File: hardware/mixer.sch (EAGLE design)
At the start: 86 parts, among them IC1 PGA2311, IC2 PGA2311, IC3 PGA2311, IC4 PGA2311, IC5 PGA2311, IC6 OPA2336U, K1 RT424F124, K2 RT424F124, Q1 si2305cd, Q3 IRLML9301, Q4 IRLML9301, Q5 IRLML9301, Q7 IRLML9301, T1 BC846, T2 BC846, T3 BC846, T4 BC846, U1 SPX5205 3v3, Y1 32768Hz CFPX-217 12.5pF

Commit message: add png
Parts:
- removed C23: 22pF, rcl:C-EUC0805
- removed D1, D2, D3, D4: M4, SparkFun-DiscreteSemi:DIODESMA
- removed K1, K2: RT424F124, relay:RT424F124
- removed LED1: green, led:LEDCHIP-LED0805
- removed LED2: orange, led:LEDCHIP-LED0805
- removed Q1: si2305cd, Simplex-DiscreteSemi:MOSFET-PCHANNELSMD_POWER
- removed Q3, Q4, Q5, Q7: IRLML9301, Simplex-DiscreteSemi:MOSFET-PCHANNELSMD_POWER
- removed R22: 8.2K, rcl:R-EU_R0805W
- removed R27: 1K, rcl:R-EU_R0805W
- removed T1, T2, T3, T4: BC846, transistor:BC846
- removed U1: SPX5205 3v3, SparkFun:V_REG_LDOSMD
- removed Y1: 32768Hz CFPX-217 12.5pF, Simplex-FreqCtrl:CRYSTAL3.2X1.5
- added C15, C16, C18, C55, C57, C59, C61, C63: 47p, rcl:C-EUC0805
- added C19, C21, C22, C25, C26, C28, C29, C30, C31, C32, C33, C34, C35, C36, C37, C38, C39, C40, C41, C42, C43, C44, C46, C47, C48, C49, C51, C52, C53, C54, C79, C80: 100n, rcl:C-EUC0805
- added C56, C58, C60, C62, C64, C65, C66, C67, C68, C69, C70, C71, C72, C73, C74, C75, C76, C77, C78: 10u, SparkFun-Capacitors:CAP_POLD
- added IC11, IC12, IC7, IC8, IC9: OPA2134P, burr-brown:OPA2134P
- added R41, R43, R45: 47K, rcl:R-EU_R0805W
- added R42, R44: 1K, rcl:R-EU_R0805W
- added U$2: INDUCTOR, Simplex-rlc:INDUCTOR
- added U$3: RESETTABLE, Simplex-Fuses:RESETTABLE
- added U$5: MOLEX_4HORIZONTAL, Simplex-Connectors:MOLEX_4HORIZONTAL
- C1, C13, C14, C5, C6, C9: value 100nF -> 100n
- C10: value 470nF -> 100n
- C11: value 220nF -> 47p
- C12, C17, C7, C8: value 100nF -> 47p
- C2, C20: value 10uF -> 100n; device rcl:C-EUC1206 -> rcl:C-EUC0805
- C24: value 22pF -> 100n
- C3: value 10uF -> 47p; device rcl:C-EUC1206 -> rcl:C-EUC0805
- C4: value 1uF -> 47p
- IC6: value OPA2336U -> OPA2134P; device burr-brown:OPA2336U -> burr-brown:OPA2134P
- R1, R11, R20, R3: value 100k -> 47K
- R12, R2, R8: value 10k -> 1K
- R13, R15, R32, R9: value 100K -> 47K
- R14: value 100K -> 1K
- R16: value 100k -> 1K
- R17: value 8K -> 22K
- R18, R24, R25, R28: value 20K -> 47K
- R19, R21: value 10k -> 47K
- R23: value 160K -> 22K
- R26: value 8K -> 47K
- R29: value 8.2K -> 22K
- R30: value 160K -> 47K
- R31: value 68K -> 10
- R33: value 50 -> 10
- R34: value 47k -> 10
- R35: value 47k -> 22K
- R36, R39: value 470 -> 47K
- R37, R38: value 470 -> 10
- R4, R6: value 4.7k -> 1K
- R40: value 50 -> 47K
- R5, R7: value 4.7k -> 47K
- U$1: value F55[0/1]X---PT48 -> INDUCTOR; device TI_MSP430_v16:F55[0/1]X---PT48 -> Simplex-rlc:INDUCTOR
- U$4: value INDUCTOR -> RESETTABLE; device Simplex-rlc:INDUCTOR -> Simplex-Fuses:RESETTABLE
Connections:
- removed net +30V: R30.2
- removed net +3V: R32.2
- removed net +3V3: C1.1, C2.1, U1.OUT
- removed net -30V: R23.2
- removed net 3V: IC6A.V+
- removed net A+3: C14.2, R31.2, R32.1, U$1.5
- removed net A+30: C13.2, R29.2, R30.1, U$1.3
- removed net A+5: C12.2, R26.2, R28.1, U$1.1
- removed net A-30: IC6B.OUT, R25.2, R9.2, U$1.4
- removed net A-5: IC6A.OUT, R13.2, R24.2, U$1.2
- removed net CHARGE_OFF: R20.2, U$1.19
- removed net CHARGE_ON: R16.2, U$1.18
- removed net CS: U$1.35
- removed net EN: R8.1, U$1.20
- removed net GND: C1.2, C10.2, C11.2, C12.1, C13.1, C14.1, C17.1, C2.2, C20.2, C23.2, C24.2, C3.2, C4.2, C5.1, C6.2, C7.1, C8.1, C9.1, IC6A.V-, LED1.C, R17.1, R22.1, R26.1, R27.1, R29.1, R31.1, R33.1, R35.2, R40.1, T1.E, T2.E, T3.E, T4.E, U$1.10, U$1.12, U$1.27, U$1.37, U$1.39, U$1.44, U1.GND
- removed net LED: R10.2, U$1.36
- removed net MISO: U$1.31
- removed net N$13: R7.2, U$1.33
- removed net N$14: Q1.G, R3.1, R8.2
- removed net N$24: C5.2, R15.1, R22.2, R23.1
- removed net N$25: C24.1, U$1.9, Y1.1
- removed net N$3: R16.1, T1.B
- removed net N$35: D3.C, K11.R+, Q7.D, R37.1
- removed net N$39: LED2.C, R27.2
- removed net N$6: C10.1, U$1.13
- removed net P1.0: U$1.14
- removed net P1.1: U$1.15
- removed net P1.2: U$1.16
- removed net P1.3: U$1.17
- removed net P4.0: U$1.29
- removed net RST: R34.1, U$1.48
- removed net RX: R6.1
- removed net R_OFF: R11.2, U$1.22
- removed net R_ON: R1.2, U$1.21
- removed net SCK: U$1.32
- removed net SCL: R4.2
- removed net SDA: R5.2
- removed net TEST: R35.1, U$1.47
- removed net TX: R7.1
- removed net VBAT: Q3.S, Q4.S, Q5.S, Q7.S, R12.1, R19.1, R2.1, R21.1
- removed net VBAT_GND: D1.A, D2.A, D3.A, D4.A, K11.-, K21.-, R36.2, R37.2, R38.2, R39.2
- removed net VCC: C17.2, C8.2, C9.2, Q1.S, R3.2, R34.2, U$1.11, U$1.28, U$1.7
- removed net VCC_EN: C20.1, R4.1, R5.1, U$4.2
- removed net VIN: C3.1, C6.1, U1.EN, U1.IN
- new net AGND: C11.1, C12.1, C15.1, C16.1, C17.1, C18.1, C29.2, C3.1, C30.2, C31.2, C34.2, C35.2, C36.2, C37.2, C38.2, C39.2, C4.1, C40.2, C41.2, C42.2, C43.2, C44.2, C46.2, C47.2, C48.2, C49.2, C51.2, C52.2, C53.2, C54.2, C65.-, C66.-, C67.-, C68.-, C69.-, C7.1, C70.+, C71.+, C72.+, C73.+, C74.+, C75.-, C76.-, C77.+, C78.+, C8.1, IC1.AGNDL, IC1.AGNDR, IC2.AGNDL, IC2.AGNDR, IC3.AGNDL, IC3.AGNDR, IC4.AGNDL, IC4.AGNDR, IC5.AGNDL, IC5.AGNDR, R1.1, R11.1, R13.1, R15.1, R17.1, R23.1, R29.1, R3.1, R35.1, R41.1, R43.1, R5.1, R7.1, R9.1, U$5.3
- new net CLK: IC1.SCLK, IC2.SCLK, IC3.SCLK, IC4.SCLK, IC5.SCLK
- new net CS1: IC1.CS
- new net CS2: IC2.CS
- new net CS3: IC3.CS
- new net CS4: IC4.CS
- new net CS5: IC5.CS
- new net DGND: C55.1, C56.-, C57.1, C58.-, C59.1, C60.-, C61.1, C62.-, C63.1, C64.-, IC1.DGND, IC2.DGND, IC3.DGND, IC4.DGND, IC5.DGND, U$5.2
- new net FRONT_L: C1.1
- new net FRONT_R: C2.1
- new net LINE_L: C9.1
- new net LINE_R: C10.1
- new net M1: IC1.MUTE
- new net M2: IC2.MUTE
- new net M3: IC3.MUTE
- new net M4: IC4.MUTE
- new net M5: IC5.MUTE
- new net M_FRONT_L: C19.1, IC11A.OUT, R18.1
- new net M_FRONT_R: C20.1, IC11B.OUT, R28.1
- new net M_REAR_L: IC12A.OUT, R30.1
- new net M_REAR_R: IC12B.OUT, R40.1
- new net N$29: IC7B.+IN
- new net N$33: C15.2, IC7A.+IN, R41.2, R42.2
- new net N$36: C17.2, IC5.VINL, R13.2, R14.2
- new net N$40: C16.2, R43.2, R44.2
- new net N$42: C19.2, R14.1
- new net N$43: C20.2, R16.1
- new net N$46: IC11A.+IN, R17.2
- new net N$47: IC11A.-IN, R18.2, R19.1, R20.1, R21.1
- new net N$48: C21.1, R19.2
- new net N$49: C24.1, R20.2
- new net N$50: C22.1, R21.2
- new net N$51: IC12B.-IN, R36.1, R40.2, R45.1
- new net N$52: IC11B.+IN, R23.2
- new net N$53: IC11B.-IN, R24.1, R25.1, R26.1, R28.2
- new net N$54: C25.1, R24.2
- new net N$55: C28.1, R25.2
- new net N$56: C26.1, R26.2
- new net N$58: IC12A.+IN, R29.2
- new net N$60: U$1.1, U$3.P$1
- new net N$61: C32.1, R32.2
- new net N$62: U$2.1, U$4.P$1
- new net N$63: U$3.P$2, U$5.1
- new net N$64: IC12B.+IN, R35.2
- new net N$66: C33.1, R36.2
- new net N$67: U$4.P$2, U$5.4
- new net N$68: IC5.VD+, R31.2
- new net N$69: C55.2, C56.+, IC1.VD+, IC1.ZCEN, R38.2
- new net N$70: C57.2, C58.+, IC2.VD+, R37.2
- new net N$71: C59.2, C60.+, IC3.VD+, R34.2
- new net N$72: C61.2, C62.+, IC4.VD+, R33.2
- new net N$73: C63.2, C64.+
- new net N$74: IC12A.-IN, R30.2, R32.1, R39.1
- new net N$75: C79.1, R39.2
- new net N$77: C80.1, R45.2
- new net REAR_L: C5.1
- new net REAR_R: C6.1
- new net SPDIF_L: C13.1
- new net SPDIF_R: C14.1
- new net V_FRONT_L: C24.2, IC1.VOUTL
- new net V_FRONT_R: C28.2, IC1.VOUTR
- new net V_LINE_L: C22.2, IC3.VOUTL
- new net V_LINE_R: C26.2, IC3.VOUTR
- new net V_REAR_L: C32.2, IC2.VOUTL
- new net V_REAR_PAN_L: C79.2, IC5.VOUTL
- new net V_REAR_PAN_R: C80.2, IC5.VOUTR
- new net V_REAR_R: C33.2, IC2.VOUTR
- new net V_SPDIF_L: C21.2, IC4.VOUTL
- new net V_SPDIF_R: C25.2, IC4.VOUTR
- net +5V: now also C29.1, C30.1, C31.1, C34.1, C35.1, C36.1, C37.1, C46.1, C47.1, C48.1, C49.1, C65.+, C66.+, C67.+, C68.+, C69.+, C75.+, C76.+, IC1.VA+, IC11A.V+, IC12A.V+, IC2.VA+, IC3.VA+, IC4.VA+, IC5.VA+, IC6A.V+, IC7A.V+, IC8A.V+, IC9A.V+, R31.1, R33.1, R34.1, R37.1, R38.1, U$1.2; no longer R28.2
- net -5V: now also C38.1, C39.1, C40.1, C41.1, C42.1, C43.1, C44.1, C51.1, C52.1, C53.1, C54.1, C70.-, C71.-, C72.-, C73.-, C74.-, C77.-, C78.-, IC1.VA-, IC11A.V-, IC12A.V-, IC2.VA-, IC3.VA-, IC4.VA-, IC5.VA-, IC6A.V-, IC7A.V-, IC8A.V-, IC9A.V-, U$2.2; no longer R18.2, R24.1, R25.1
- net MOSI: now also IC1.SDI, IC2.SDI, IC3.SDI, IC4.SDI, IC5.SDI; no longer U$1.30
- net N$1: now also C1.2, R42.1; no longer LED1.A, R10.1
- net N$10: now also C4.2, R3.2, R4.2; no longer Q3.G, R2.2, T2.C
- net N$11: now also C5.2, R2.1; no longer R6.2, U$1.34
- net N$12: now also C6.2, R4.1; no longer D1.C, K21.S+, Q3.D, R38.1
- net N$15: now also IC3.VINL, IC8A.-IN, IC8A.OUT; no longer R11.1, T4.B
- net N$16: now also IC3.VINR, IC8B.-IN, IC8B.OUT; no longer Q5.G, R12.2, T4.C
- net N$17: now also IC7B.-IN, IC7B.OUT
- net N$18: now also IC8B.+IN; no longer D4.C, K21.R+, Q5.D, R36.1
- net N$19: now also IC9A.-IN, IC9A.OUT; no longer IC2.VINL, IC2.VINR, IC2.VOUTL, IC2.VOUTR, IC3.VINL, IC3.VINR, IC3.VOUTL, IC3.VOUTR, IC4.VINR, IC4.VOUTL, IC4.VOUTR, IC5.VINL, IC5.VINR, IC5.VOUTL, IC5.VOUTR
- net N$2: now also C2.2, R44.1; no longer C4.1, U1.BP
- net N$20: now also C7.2, IC8A.+IN, R5.2, R6.2; no longer IC6A.-IN, R13.1, R14.2
- net N$21: now also C8.2, R7.2, R8.2; no longer IC6B.-IN, R15.2, R9.1
- net N$22: now also C9.2, R6.1; no longer IC6A.+IN, R33.2
- net N$23: now also C10.2, R8.1; no longer IC6B.+IN, R40.2
- net N$26: now also IC4.VINR, IC9B.-IN, IC9B.OUT; no longer C23.1, U$1.8, Y1.2
- net N$27: now also IC9B.+IN; no longer C7.2, R14.1, R17.2, R18.1
- net N$28: now also C11.2, IC9A.+IN, R10.2, R9.2; no longer Q4.G, R19.2, T1.C
- net N$30: now also C12.2, R11.2, R12.2; no longer D2.C, K11.S+, Q4.D, R39.1
- net N$31: now also C13.2, R10.1; no longer R20.1, T3.B
- net N$32: now also C14.2, R12.1; no longer Q7.G, R21.2, T3.C
- net N$37: now also C18.2, IC5.VINR, R15.2, R16.2; no longer Q1.D, U$4.1
- net N$4: now also IC2.VINL, IC6A.-IN, IC6A.OUT; no longer IC1.VOUTL
- net N$5: now also IC7A.-IN, IC7A.OUT
- net N$7: now also IC2.VINR, IC6B.-IN, IC6B.OUT; no longer C11.1, U$1.43
- net N$8: now also IC6B.+IN; no longer R1.1, T2.B
- net N$9: now also C3.2, IC6A.+IN, R1.2, R2.2; no longer IC1.VOUTR
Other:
- note added: "front"
- note added: "front to rear pan"
- note added: "line in"
- note added: "rear"
- note added: "spdif"
- note removed: "uC pins: 7 11 28"
- moved on the sheet: C1, C10, C11, C12, C13, C14, C17, C2, C20, C24, C3, C4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

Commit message: power tweaked
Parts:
- removed C55, C57, C59, C61, C63: 47p, rcl:C-EUC0805
- removed C56, C58, C60, C62, C64: 10u, SparkFun-Capacitors:CAP_POLD
- removed R31, R33, R34, R37, R38: 10, rcl:R-EU_R0805W
- added C45, C50, C81, C82, C83, C84, C85, C86: 100n, rcl:C-EUC0805
- added C87, C88, C89, C90, C91, C94: 10u, SparkFun-Capacitors:CAP_POLD
- added U$10, U$8: RESETTABLE, Simplex-Fuses:RESETTABLE
- added U$6, U$9: bead, Simplex-rlc:INDUCTOR
- U$1, U$2: value INDUCTOR -> bead
- U$5: value MOLEX_4HORIZONTAL -> MOLEX_6HORIZONTAL; device Simplex-Connectors:MOLEX_4HORIZONTAL -> Simplex-Connectors:MOLEX_6HORIZONTAL
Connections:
- net -5V renamed A-5V
- removed net N$10: C4.2, R3.2, R4.2
- removed net N$21: C8.2, R7.2, R8.2
- removed net N$30: C12.2, R11.2, R12.2
- removed net N$40: C16.2, R43.2, R44.2
- removed net N$67: U$4.P$2, U$5.4
- removed net N$68: IC5.VD+, R31.2
- removed net N$69: C55.2, C56.+, IC1.VD+, IC1.ZCEN, R38.2
- removed net N$70: C57.2, C58.+, IC2.VD+, R37.2
- removed net N$71: C59.2, C60.+, IC3.VD+, R34.2
- removed net N$72: C61.2, C62.+, IC4.VD+, R33.2
- removed net N$73: C63.2, C64.+
- new net +3V: C84.1, C85.1, C86.1, C87.-, U$9.2
- new net A+5V: C29.1, C30.1, C31.1, C34.1, C35.1, C36.1, C37.1, C46.1, C47.1, C48.1, C49.1, C65.+, C66.+, C67.+, C68.+, C69.+, C75.+, C76.+, IC1.VA+, IC11A.V+, IC12A.V+, IC2.VA+, IC3.VA+, IC4.VA+, IC5.VA+, IC6A.V+, IC7A.V+, IC8A.V+, IC9A.V+, U$1.2
- new net N$24: U$4.P$2, U$5.3
- new net N$25: U$5.4, U$8.P$2
- new net N$3: U$6.1, U$8.P$1
- new net N$34: U$10.P$2, U$5.5
- new net N$6: U$10.P$1, U$9.1
- net +5V: now also C45.1, C50.1, C81.1, C82.1, C83.1, C88.-, C89.-, C90.-, C91.-, C94.-, IC1.VD+, IC1.ZCEN, IC2.VD+, IC2.ZCEN, IC3.VD+, IC3.ZCEN, IC4.VD+, IC4.ZCEN, IC5.VD+, IC5.ZCEN, U$6.2; no longer C29.1, C30.1, C31.1, C34.1, C35.1, C36.1, C37.1, C46.1, C47.1, C48.1, C49.1, C65.+, C66.+, C67.+, C68.+, C69.+, C75.+, C76.+, IC1.VA+, IC11A.V+, IC12A.V+, IC2.VA+, IC3.VA+, IC4.VA+, IC5.VA+, IC6A.V+, IC7A.V+, IC8A.V+, IC9A.V+, R31.1, R33.1, R34.1, R37.1, R38.1, U$1.2
- net AGND: now also U$5.1; no longer U$5.3
- net DGND: now also C45.2, C50.2, C81.2, C82.2, C83.2, C84.2, C85.2, C86.2, C87.+, C88.+, C89.+, C90.+, C91.+, C94.+, U$5.6; no longer C55.1, C56.-, C57.1, C58.-, C59.1, C60.-, C61.1, C62.-, C63.1, C64.-, U$5.2
- net M_FRONT_L: now also C20.1; no longer C19.1
- net M_FRONT_R: now also C19.1; no longer C20.1
- net N$18: now also C8.2, R7.2, R8.2
- net N$27: now also C12.2, R11.2, R12.2
- net N$29: now also C16.2, R43.2, R44.2
- net N$63: now also U$5.2; no longer U$5.1
- net N$8: now also C4.2, R3.2, R4.2
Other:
- moved on the sheet: C21, C22, C24, C25, C26, C28, C29, C30, C31, C32, C33, C34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

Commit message: add msp
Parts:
- added C23: 470nF, rcl:C-EUC0805
- added C27: 220nF, rcl:C-EUC0805
- added C55, C56: 22pF, rcl:C-EUC0805
- added LED2: green, led:LEDCHIPLED_0805
- added R22, R27: 4.7k, rcl:R-EU_R0805W
- added R31, R34: 47k, rcl:R-EU_R0805W
- added R33: 100k, rcl:R-EU_R0805W
- added U$11: F55[0/1]X---PT48, TI_MSP430_v16:F55[0/1]X---PT48
- added U$12: prog, Simplex-Connectors:MOLEX_6HORIZONTAL
- added Y1: 32768Hz CFPX-217 12.5pF, Simplex-FreqCtrl:CRYSTAL3.2X1.5
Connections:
- new net GND: C23.2, C27.2, C55.2, C56.2, R31.2, R33.1, U$11.10, U$11.12, U$11.27, U$11.37, U$11.44, U$12.1
- new net N$10: C23.1, U$11.13
- new net N$13: C27.1, U$11.43
- new net N$14: R22.2, U$11.34
- new net N$21: R27.2, U$11.33
- new net N$30: C56.1, U$11.9, Y1.1
- new net N$35: C55.1, U$11.8, Y1.2
- new net N$38: LED2.C, R33.2
- new net N$39: LED2.A, U$11.22
- new net RST: R34.1, U$11.48, U$12.2
- new net RX: R22.1, U$12.5
- new net TEST: R31.1, U$11.47, U$12.3
- new net TX: R27.1, U$12.6
- new net VCC: R34.2, U$11.11, U$11.28, U$11.7, U$12.4
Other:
- moved on the sheet: C65, C66, C67, C68, C69, C70, C71, C72, C73, C74, C75, C76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

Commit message: change C footprints
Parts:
- removed C94: 10u, SparkFun-Capacitors:CAP_POLD
- removed U$12: prog, Simplex-Connectors:MOLEX_6HORIZONTAL
- removed U$5: MOLEX_6HORIZONTAL, Simplex-Connectors:MOLEX_6HORIZONTAL
- added C57: 100nF, rcl:C-EUC0805
- added C58, C59, C60, C61, C62: 100n, rcl:C-EUC0805
- added C64: 10u, rcl:CPOL-EU153CLV-0405
- added Q1: SI2305, Simplex-DiscreteSemi:MOSFET-PCHANNEL_SOT23-3_POWER
- added Q2: MOSFET-NCHANNEL_SOT23-3, Simplex-DiscreteSemi:MOSFET-NCHANNEL_SOT23-3
- added R37, R38, R46: 10K, rcl:R-EU_R0805W
- added R47, R48, R49, R50, R51: 47K, rcl:R-EU_R0805W
- added X1: MOLEX_6HORIZONTAL, Simplex-Connectors:MOLEX_6HORIZONTAL
- added X2: MOLEX_6VERTICAL, Simplex-Connectors:MOLEX_6VERTICAL
- added X3: MOLEX_4VERTICAL, Simplex-Connectors:MOLEX_4VERTICAL
- C65, C66, C67, C68, C69, C70, C71, C72, C73, C74, C75, C76, C77, C78, C87, C88, C89, C90, C91: device SparkFun-Capacitors:CAP_POLD -> rcl:CPOL-EU153CLV-0405
- R22, R27: value 4.7k -> 2.2K
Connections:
- removed net +5V: C45.1, C50.1, C81.1, C82.1, C83.1, C88.-, C89.-, C90.-, C91.-, C94.-, IC1.VD+, IC1.ZCEN, IC2.VD+, IC2.ZCEN, IC3.VD+, IC3.ZCEN, IC4.VD+, IC4.ZCEN, IC5.VD+, IC5.ZCEN, U$6.2
- removed net GND: C23.2, C27.2, C55.2, C56.2, R31.2, R33.1, U$11.10, U$11.12, U$11.27, U$11.37, U$11.44, U$12.1
- new net +5V_DIG: Q1.S, R37.2, U$6.2
- new net +5V_PGA: C45.1, C50.1, C57.2, C78.+, C81.1, C82.1, C83.1, C88.+, C89.+, C90.+, C91.+, IC1.VD+, IC1.ZCEN, IC2.VD+, IC2.ZCEN, IC3.VD+, IC3.ZCEN, IC4.VD+, IC4.ZCEN, IC5.VD+, IC5.ZCEN, Q1.D
- new net N$40: C57.1, Q1.G, Q2.D, R37.1
- new net N$41: Q2.G, R38.2, R46.1
- new net N$44: IC1.SDO, R49.1
- new net N$45: IC3.SDO, R47.1
- new net N$57: IC2.SDO, R48.1
- new net N$59: IC4.SDO, R50.1
- new net N$65: IC5.SDO, R51.1
- new net PGA_EN: R46.2
- net +3V: now also C87.+; no longer C87.-
- net A+5V: now also C58.2, C59.2, C60.2, C61.2, C62.2, C64.+, C70.+; no longer C75.+, C76.+
- net A-5V: now also C58.1, C59.1, C60.1, C61.1, C62.1, C75.-, C76.-; no longer C70.-, C78.-
- net AGND: now also C64.-, C70.-, C75.+, C76.+, X2.1; no longer C70.+, C75.-, C76.-, C78.+, U$5.1
- net DGND: now also C23.2, C27.2, C55.2, C56.2, C78.-, C87.-, C88.-, C89.-, C90.-, C91.-, Q2.S, R31.2, R33.1, R38.1, R47.2, R48.2, R49.2, R50.2, R51.2, U$11.10, U$11.12, U$11.27, U$11.37, U$11.44, X1.1, X2.6, X3.1, X3.4; no longer C87.+, C88.+, C89.+, C90.+, C91.+, C94.+, U$5.6
- net N$24: now also X2.3; no longer U$5.3
- net N$25: now also X2.4; no longer U$5.4
- net N$34: now also X2.5; no longer U$5.5
- net N$63: now also X2.2; no longer U$5.2
- net RST: now also X1.2; no longer U$12.2
- net RX: now also X1.5, X3.2; no longer U$12.5
- net TEST: now also X1.3; no longer U$12.3
- net TX: now also X1.6, X3.3; no longer U$12.6
- net VCC: now also X1.4; no longer U$12.4
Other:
- moved on the sheet: C65, C66, C67, C68, C69, C70, C71, C72, C73, C74, C75, C76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

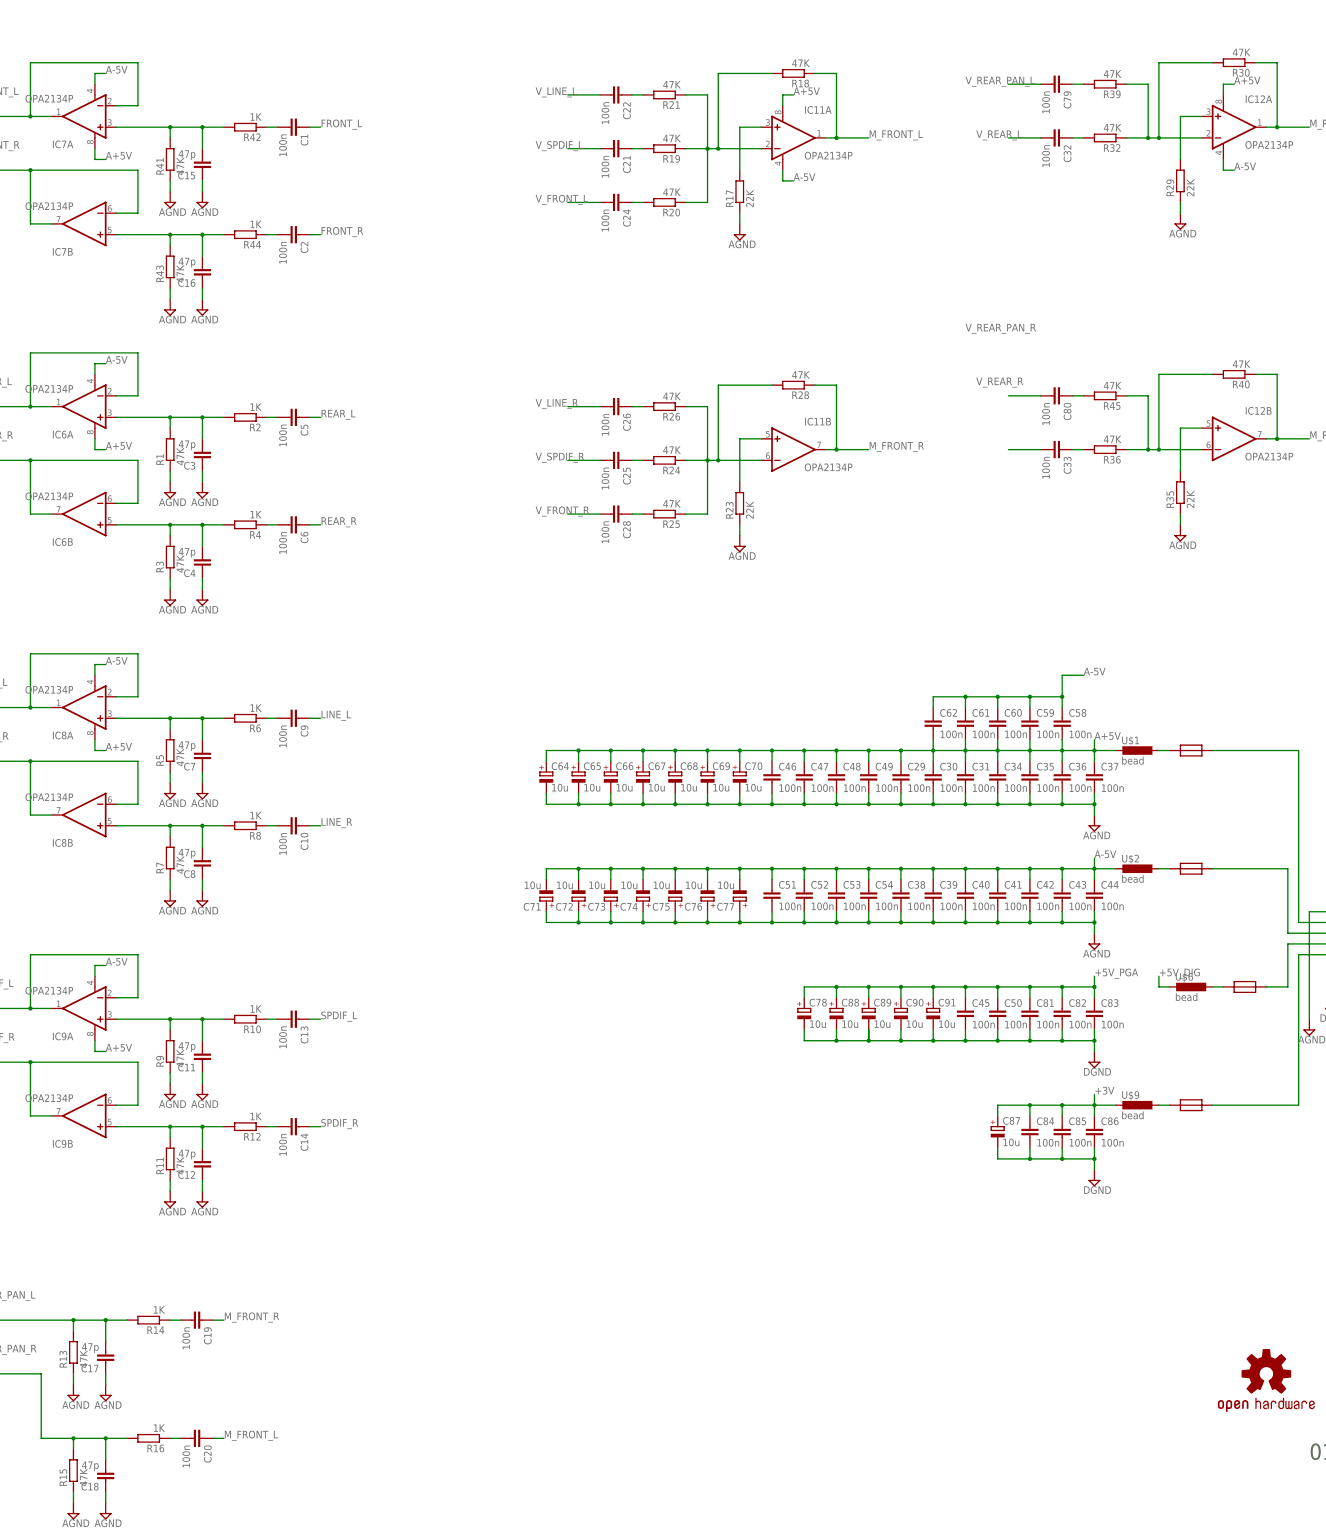
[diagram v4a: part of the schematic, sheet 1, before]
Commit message: change input filters
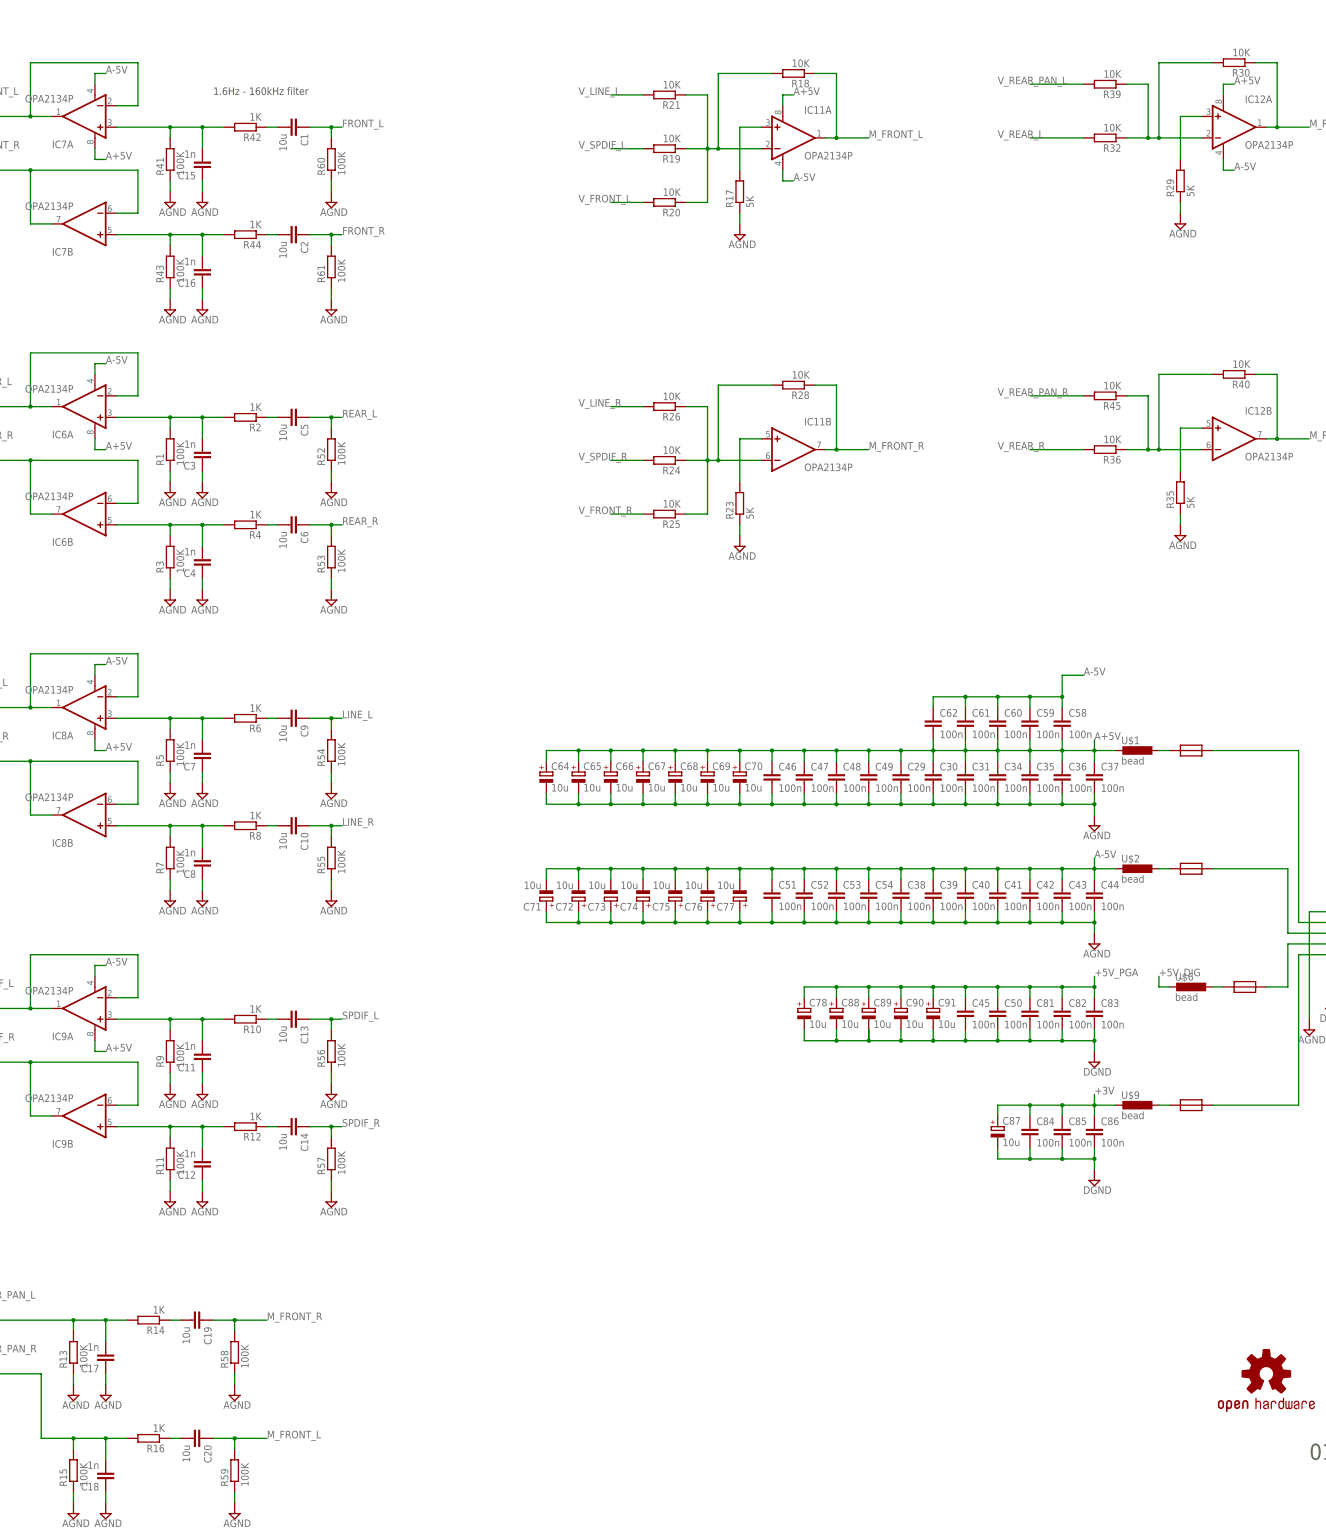
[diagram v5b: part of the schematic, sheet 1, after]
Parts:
- removed C21, C22, C24, C25, C26, C28, C32, C33, C79, C80: 100n, rcl:C-EUC0805
- added R52, R53, R54, R55, R56, R57, R58, R59, R60, R61: 100K, rcl:R-EU_R0805W
- C1, C10, C13, C14, C19, C2, C20, C5, C6, C9: value 100n -> 10u
- C11, C12, C15, C16, C17, C18, C3, C4, C7, C8: value 47p -> 1n
- R1, R11, R13, R15, R3, R41, R43, R5, R7, R9: value 47K -> 100K
- R17, R23, R29, R35: value 22K -> 5K
- R18, R19, R20, R21, R24, R25, R26, R28, R30, R32, R36, R39, R40, R45: value 47K -> 10K
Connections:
- removed net N$48: C21.1, R19.2
- removed net N$49: C24.1, R20.2
- removed net N$50: C22.1, R21.2
- removed net N$54: C25.1, R24.2
- removed net N$55: C28.1, R25.2
- removed net N$56: C26.1, R26.2
- removed net N$61: C32.1, R32.2
- removed net N$66: C33.1, R36.2
- removed net N$75: C79.1, R39.2
- removed net N$77: C80.1, R45.2
- net AGND: now also R52.1, R53.1, R54.1, R55.1, R56.1, R57.1, R58.1, R59.1, R60.1, R61.1
- net FRONT_L: now also R60.2
- net FRONT_R: now also R61.2
- net LINE_L: now also R54.2
- net LINE_R: now also R55.2
- net M_FRONT_L: now also R59.2
- net M_FRONT_R: now also R58.2
- net REAR_L: now also R52.2
- net REAR_R: now also R53.2
- net SPDIF_L: now also R56.2
- net SPDIF_R: now also R57.2
- net V_FRONT_L: now also R20.2; no longer C24.2
- net V_FRONT_R: now also R25.2; no longer C28.2
- net V_LINE_L: now also R21.2; no longer C22.2
- net V_LINE_R: now also R26.2; no longer C26.2
- net V_REAR_L: now also R32.2; no longer C32.2
- net V_REAR_PAN_L: now also R39.2; no longer C79.2
- net V_REAR_PAN_R: now also R45.2; no longer C80.2
- net V_REAR_R: now also R36.2; no longer C33.2
- net V_SPDIF_L: now also R19.2; no longer C21.2
- net V_SPDIF_R: now also R24.2; no longer C25.2
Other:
- note added: "1.6Hz - 160kHz filter"
